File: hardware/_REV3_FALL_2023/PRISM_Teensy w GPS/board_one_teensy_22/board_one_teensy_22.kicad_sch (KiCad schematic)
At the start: 31 parts, among them J1 Micro_SD_Card_Det_Hirose_DM3AT, J3 3387, Q1 AO3400A, Q2 AO3400A, U1 Teensy4.0, U2 GPS-14414, U3 3966, U4 RFM69HCW_Breakout, U5 CT25E-16T150-1, U6 CMI-9605-1280T

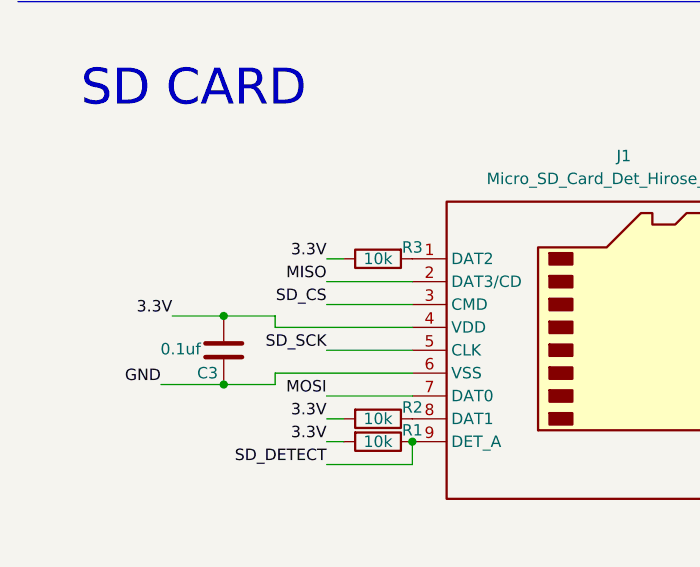
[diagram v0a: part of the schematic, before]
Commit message: Added Missing holes on CoreIO
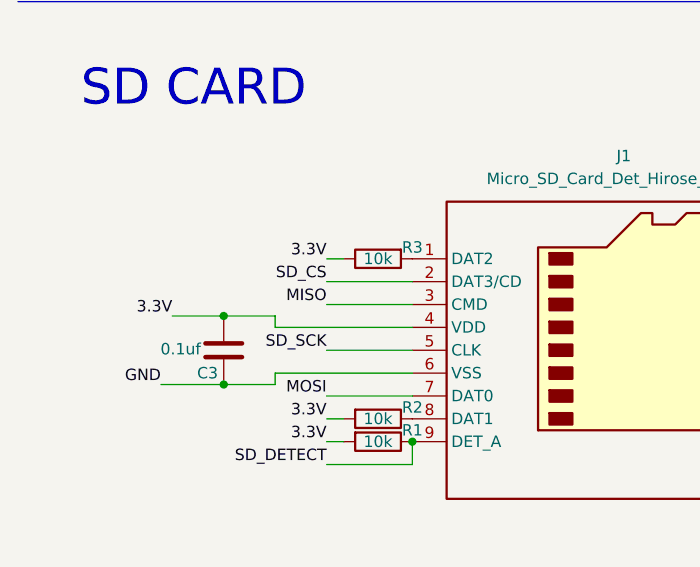
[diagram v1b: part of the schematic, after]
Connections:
- net MISO: now also J1.3 (CMD); no longer J1.2 (DAT3/CD)
- net SD_CS: now also J1.2 (DAT3/CD); no longer J1.3 (CMD)
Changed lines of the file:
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@@
-    (effects (font (size 1.27 1.27)) (justify right bottom))
-  )
-  (label "SD_CS" (at 46.355 162.56 180) (fields_autoplaced)
     (effects (font (size 1.27 1.27)) (justify right bottom))
   )
@@
     (effects (font (size 1.27 1.27)) (justify right bottom))
   )
+  (label "SD_CS" (at 46.355 160.02 180) (fields_autoplaced)
+    (effects (font (size 1.27 1.27)) (justify right bottom))
+  )
   (label "3.3V" (at 132.08 95.25 180) (fields_autoplaced)
     (effects (font (size 1.27 1.27)) (justify right bottom))
@@
   (label "GND" (at 267.97 79.248 0) (fields_autoplaced)
     (effects (font (size 1.27 1.27)) (justify left bottom))
+  )
+  (label "MISO" (at 46.355 162.56 180) (fields_autoplaced)
+    (effects (font (size 1.27 1.27)) (justify right bottom))
   )
   (label "SCL" (at 133.35 100.33 180) (fields_autoplaced)
@@
     (effects (font (size 1.27 1.27)) (justify right bottom))
   )
-  (label "MISO" (at 46.355 160.02 180) (fields_autoplaced)
-    (effects (font (size 1.27 1.27)) (justify right bottom))
-  )
